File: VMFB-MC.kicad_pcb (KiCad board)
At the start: 2 copper layers, 79.1 x 83 mm, 52 parts, among them J1 DISPENSE, J12 Conn_01x10_Pin, J2 EMPTY, J3 DISPENSE, J4 DEPOSIT, J5 DISPENSE, J6 EMPTY, J7 MOTOR, J8 PIR, J9 Conn_01x04_Pin, Q1 Q_Photo_NPN, Q10 Q_Photo_NPN, Q2 Q_Photo_NPN, Q3 Q_Photo_NPN, Q4 Q_Photo_NPN, Q5 Q_Photo_NPN, Q6 Q_Photo_NPN, Q7 TIP120, Q8 TIP120, Q9 BC337, U1 LM393

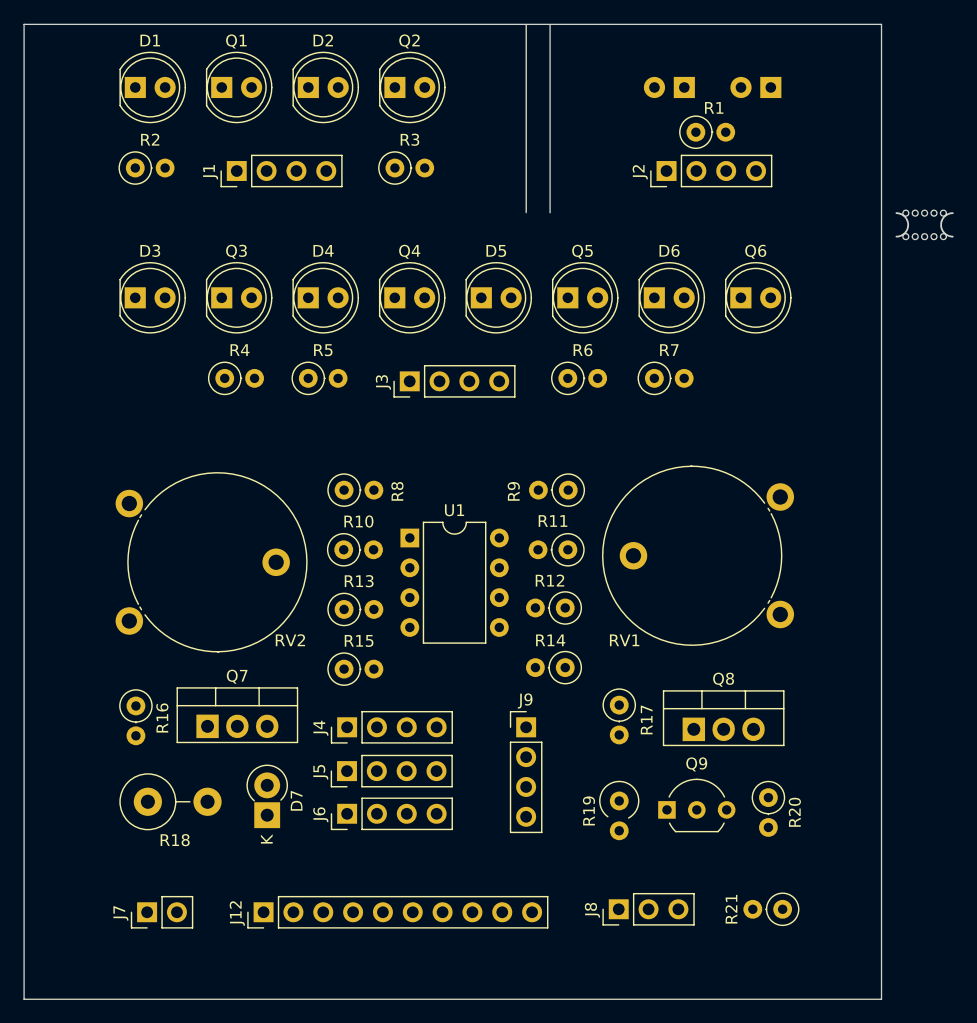
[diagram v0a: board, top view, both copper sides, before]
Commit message: New layour and routing
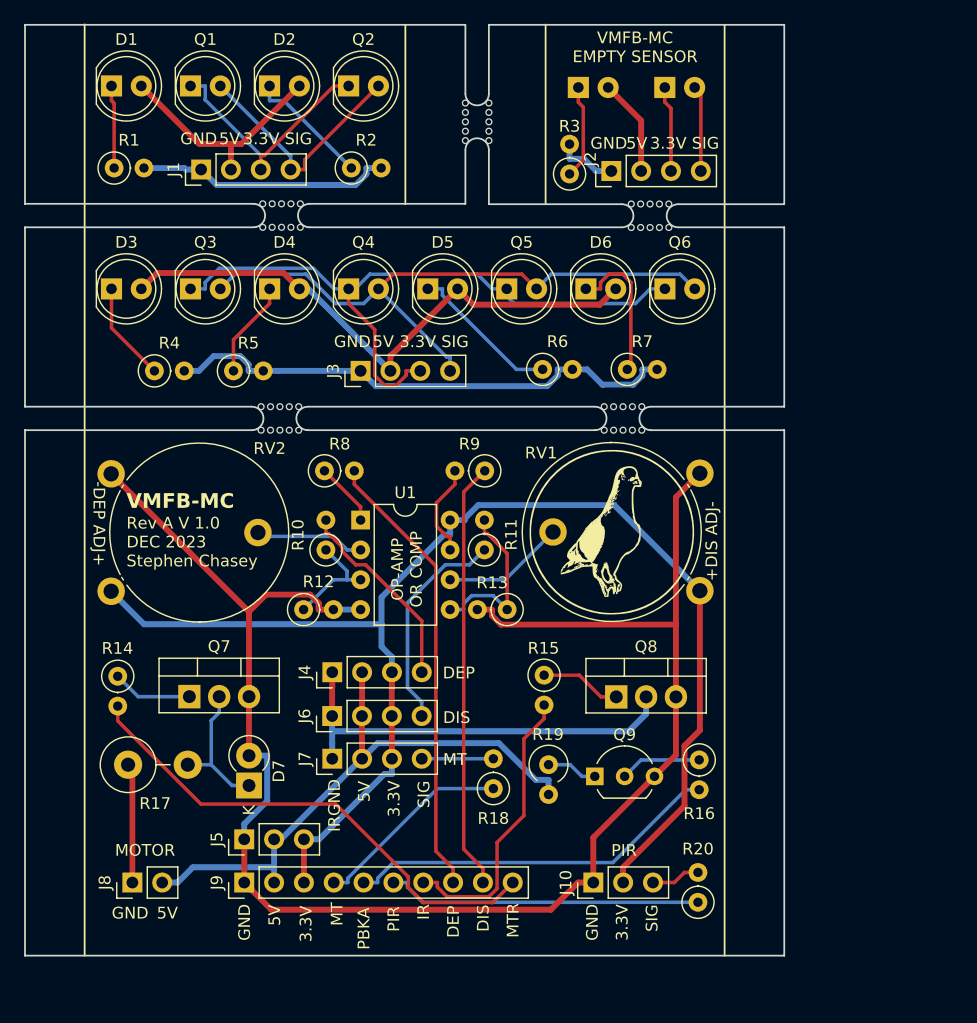
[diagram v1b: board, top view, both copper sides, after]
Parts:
- removed the J9 at (142.7, 109.8)
- removed the R10 at (127.2, 94.7)
- removed the R11 at (146.3, 94.7)
- added J5: Conn_01x03_Pin, Connector_PinHeader_2.54mm:PinHeader_1x03_P2.54mm_Vertical, F.Cu at (118.7, 119.4)
- added LOGO_BACK: LOGO, VMFB:VMFB_logo_14mm, B.Cu at (150.1, 93.2)
- added LOGO_FRONT: LOGO, VMFB:VMFB_logo_14mm, F.Cu at (150.0, 93.2)
- added R18: 10K, Resistor_THT:R_Axial_DIN0207_L6.3mm_D2.5mm_P2.54mm_Vertical, F.Cu at (140.0, 115.1)
- moved R3 11.3 mm to (146.4, 62.7), turned to 90 degrees
- moved Q10 9.03 mm to (154.5, 55.4), turned to 0 degrees
- moved D8 9.02 mm to (147.2, 55.4), turned to 0 degrees
- moved R11 8.47 mm to (139.2, 94.7), turned to 90 degrees
- moved R9 7.29 mm to (139.2, 88.0)
- moved R20 7.24 mm to (157.4, 124.7), turned to 90 degrees
- moved Q8 7.16 mm to (150.4, 107.3)
- moved RV1 7.14 mm to (157.5, 88.2)
- moved R13 6.99 mm to (141.1, 99.8)
- moved R15 6.89 mm to (144.3, 105.4)
- moved Q9 6.78 mm to (148.6, 114.0)
- moved R19 6.76 mm to (144.7, 113.0)
- moved R16 6.71 mm to (157.5, 112.6)
- moved Q6 6.51 mm to (154.6, 72.5)
- moved R5 6.40 mm to (117.8, 79.5)
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- renumbered J8 to J10, J5 to J6, J6 to J7, J7 to J8, J12 to J9, R2 to R1, R13 to R10, R12 to R11, R15 to R12, R14 to R13, R16 to R14, R17 to R15, R20 to R16, R18 to R17, R3 to R2, R21 to R20, R1 to R3
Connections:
- net Net-(D1-A) renamed DIS PWR
- net Net-(D3-A) renamed DEP PWR
- net Net-(D8-A) renamed MT PWR
- net Net-(J1-Pin_1) renamed DIS GND
- net Net-(J2-Pin_1) renamed MT GND
- net Net-(J3-Pin_1) renamed DEP GND
- J7 pad 4: EMPTY -> Net-(J7-Pin_4)
- J9 pad 2: +3.3V -> +5V
- J9 pad 3: +5V -> +3.3V
- R13 pad 1: GND -> Net-(U1B-+)
- R13 pad 2: Net-(U1B-+) -> GND
- R17 pad 1: Net-(D7-K) -> MOTOR GND
- R17 pad 2: MOTOR GND -> Net-(D7-K)
- RV1 pad 1: +3.3V -> GND
- RV1 pad 3: GND -> +3.3V
- U1 pad 2: Net-(U1A--) -> DEPOSIT ADJ
- U1 pad 6: Net-(U1B--) -> DISPENSE ADJ
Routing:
- net GND: track 0.00 -> 140.9 mm
- net +3.3V: track 0.00 -> 114.8 mm
- net Net-(J3-Pin_3): track 0.00 -> 58.1 mm
- net Net-(J3-Pin_4): track 0.00 -> 54.2 mm
- net +5V: track 0.00 -> 50.7 mm
- net DEP PWR: track 0.00 -> 49.2 mm
- net DEP GND: track 0.00 -> 44.4 mm
- net MOTOR: track 0.00 -> 42.5 mm
- net DEPOSIT: track 0.00 -> 38.5 mm
- net DISPENSE: track 0.00 -> 36.5 mm
- net IR GND: track 0.00 -> 36.2 mm
- net PBKA: track 0.00 -> 32.1 mm
- net PIR: track 0.00 -> 26.8 mm
- net SENSOR IR: track 0.00 -> 24.6 mm
- net DIS GND: track 0.00 -> 21.7 mm
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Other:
- board size 79.1 x 83 mm -> 64.6 x 79.2 mm
- board text added: "+DIS ADJ-"
- board text added: "-DEP ADJ+"
- board text added: "3.3V"
- board text added: "5V"
- board text added: "DEP"
- board text added: "DIS"
- board text added: "GND"
- board text added: "IR"
- board text added: "IRGND"
- board text added: "MOTOR"
- board text added: "MT"
- board text added: "MTR"
- board text added: "OP-AMP OR COMP"
- board text added: "PBKA"
- board text added: "PIR"
- board text added: "Rev A V 1.0 DEC 2023 Stephen Chasey"
- board text added: "SIG"
- board text added: "VMFB-MC"
- board text added: "VMFB-MC DEPOSIT SENSOR"
- board text added: "VMFB-MC DISPENSE SENSOR"
- board text added: "VMFB-MC EMPTY SENSOR"
- board text added: "VMFB-MC MAIN BOARD"

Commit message: updating netclasses, adding routing
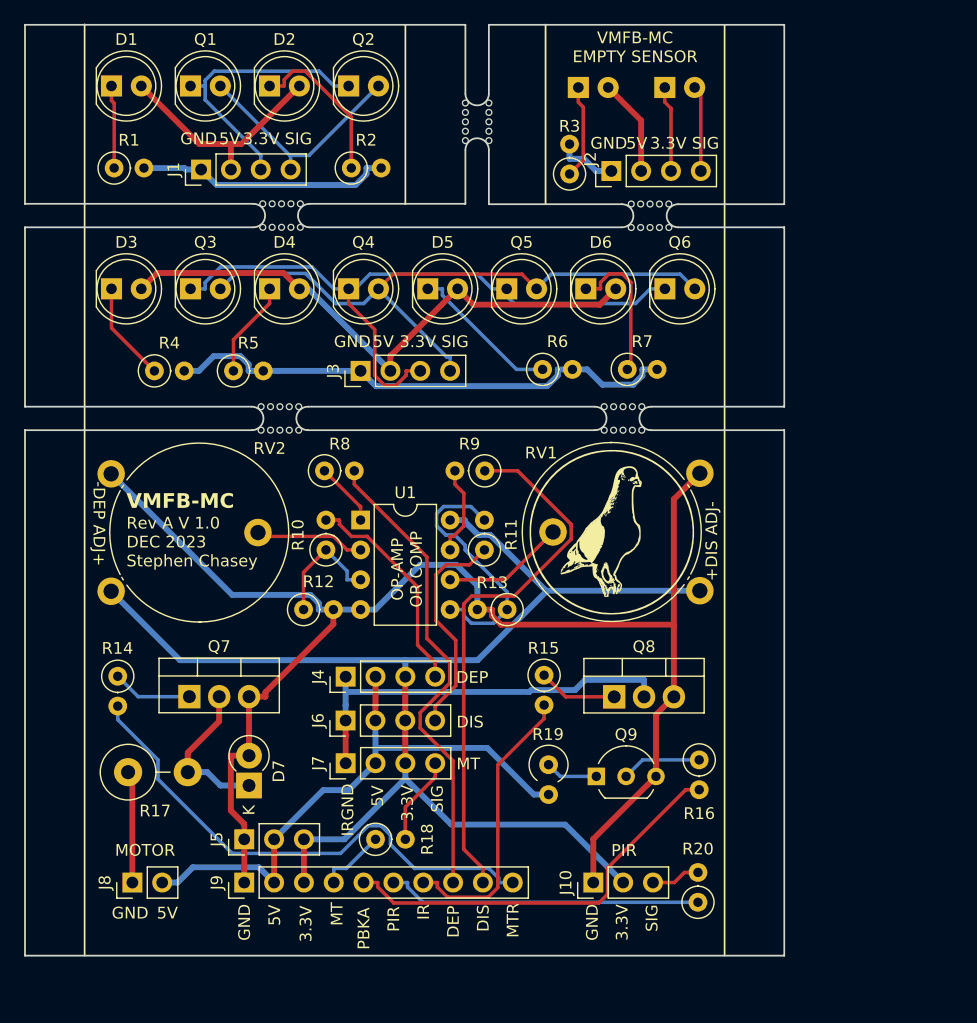
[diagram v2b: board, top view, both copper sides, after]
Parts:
- moved R18 10.9 mm to (129.9, 119.4), turned to 0 degrees
- moved J4 1.20 mm to (127.4, 105.5)
- moved J6 1.20 mm to (127.4, 109.3)
- moved J7 1.20 mm to (127.4, 112.9)
- moved R17 0.64 mm to (108.9, 113.7)
- moved Q8 0.18 mm to (150.2, 107.3)
- moved Q9 0.13 mm to (148.7, 114.0)
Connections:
- net Net-(D7-K) renamed MOTOR GND RES
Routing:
- net GND: track 140.9 -> 126.2 mm
- net EMPTY: track 17.1 -> 5.78 mm
- net DISPENSE: track 36.5 -> 46.3 mm
- net Net-(U1B-+): track 14.7 -> 22.0 mm
- net Net-(D2-K): track 10.6 -> 13.8 mm
- net PBKA: track 32.1 -> 34.8 mm
- net Net-(J1-Pin_3): track 21.4 -> 23.9 mm
- net +3.3V: track 114.8 -> 112.5 mm
- net DEPOSIT: track 38.5 -> 40.6 mm
- net DEPOSIT SIG: track 17.0 -> 18.6 mm
- net MOTOR: track 42.5 -> 44.1 mm
- net IR GND: track 36.2 -> 34.7 mm
- net Net-(J7-Pin_4): track 6.10 -> 7.53 mm
- net +5V: track 50.7 -> 49.4 mm
- net MOTOR GND RES: track 12.0 -> 13.2 mm
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
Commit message: cleaned up tracks
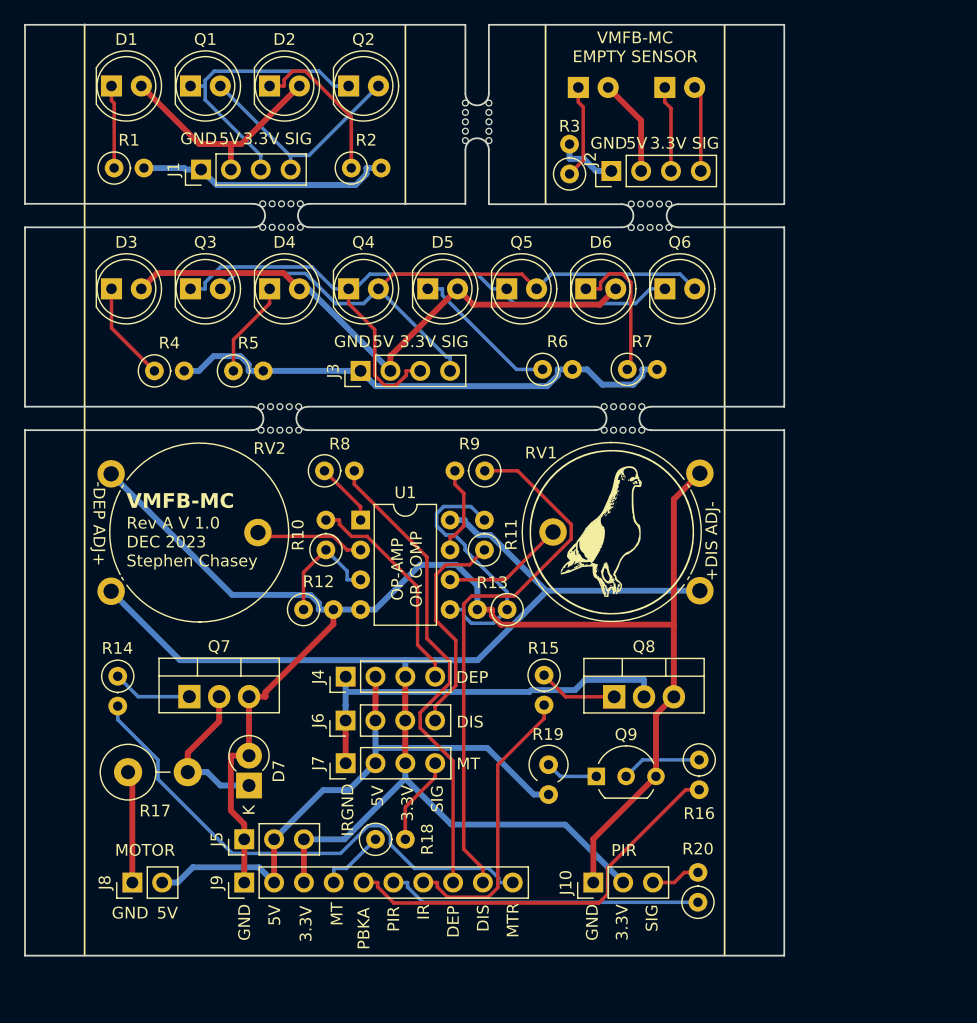
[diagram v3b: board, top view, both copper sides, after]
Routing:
- net Net-(J3-Pin_3): track 58.2 -> 57.0 mm
- net MOTOR GND: track 9.55 -> 9.03 mm
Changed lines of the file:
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@@
     (effects (font (size 1 1) (thickness 0.15)) (justify left bottom))
   )
-  (segment (start 108.856 113.665) (end 109.22 114.029) (width 0.5) (layer "F.Cu") (net 1))
   (segment (start 109.22 114.029) (end 109.22 123.063) (width 0.5) (layer "F.Cu") (net 1))
   (segment (start 119.882 107.2355) (end 120.5536 107.2355) (width 0.5) (layer "F.Cu") (net 2))
@@
   (segment (start 149.0781 72.517) (end 149.0781 71.9701) (width 0.3) (layer "F.Cu") (net 5))
   (segment (start 149.8048 71.2434) (end 150.9316 71.2434) (width 0.3) (layer "F.Cu") (net 5))
-  (segment (start 151.6608 79.0692) (end 151.355 79.375) (width 0.3) (layer "F.Cu") (net 5))
   (segment (start 147.828 72.517) (end 149.0781 72.517) (width 0.3) (layer "F.Cu") (net 5))
   (segment (start 149.0781 71.9701) (end 149.8048 71.2434) (width 0.3) (layer "F.Cu") (net 5))
@@
   (segment (start 128.651 94.742) (end 127.5009 94.742) (width 0.3) (layer "F.Cu") (net 19))
   (segment (start 126.3508 93.5919) (end 120.2394 93.5919) (width 0.3) (layer "F.Cu") (net 19))
-  (segment (start 120.2394 93.5919) (end 119.913 93.2655) (width 0.3) (layer "F.Cu") (net 19))
   (segment (start 139.065 123.063) (end 139.065 121.8629) (width 0.3) (layer "F.Cu") (net 20))
   (segment (start 138.1058 98.6718) (end 141.7381 98.6718) (width 0.3) (layer "F.Cu") (net 20))
@@
   (segment (start 107.442 56.4951) (end 107.667 56.7201) (width 0.3) (layer "F.Cu") (net 26))
   (segment (start 107.442 55.245) (end 107.442 56.4951) (width 0.3) (layer "F.Cu") (net 26))
-  (segment (start 117.612 61.0569) (end 117.612 60.1872) (width 0.5) (layer "F.Cu") (net 27))
+  (segment (start 117.612 62.357) (end 117.612 60.1872) (width 0.5) (layer "F.Cu") (net 27))
   (segment (start 118.4968 60.1872) (end 117.612 60.1872) (width 0.5) (layer "F.Cu") (net 27))
   (segment (start 123.439 55.245) (end 118.4968 60.1872) (width 0.5) (layer "F.Cu") (net 27))
-  (segment (start 117.612 62.357) (end 117.612 61.0569) (width 0.5) (layer "F.Cu") (net 27))
   (segment (start 114.9242 60.1872) (end 109.982 55.245) (width 0.5) (layer "F.Cu") (net 27))
   (segment (start 117.612 60.1872) (end 114.9242 60.1872) (width 0.5) (layer "F.Cu") (net 27))
@@
   (segment (start 152.6449 79.893) (end 152.6449 79.375) (width 0.5) (layer "B.Cu") (net 38))
   (segment (start 145.4349 79.893) (end 145.4349 79.375) (width 0.5) (layer "B.Cu") (net 38))
-  (segment (start 128.651 79.502) (end 121.6171 79.502) (width 0.5) (layer "B.Cu") (net 38))
+  (segment (start 120.367 79.502) (end 128.651 79.502) (width 0.5) (layer "B.Cu") (net 38))
   (segment (start 153.895 79.375) (end 152.6449 79.375) (width 0.5) (layer "B.Cu") (net 38))
-  (segment (start 120.367 79.502) (end 121.6171 79.502) (width 0.5) (layer "B.Cu") (net 38))
   (segment (start 130.7102 80.741) (end 129.8512 79.882) (width 0.3) (layer "F.Cu") (net 39))
   (segment (start 129.8512 79.882) (end 129.8512 75.9883) (width 0.3) (layer "F.Cu") (net 39))
@@
   (segment (start 133.731 79.502) (end 132.5309 79.502) (width 0.3) (layer "F.Cu") (net 39))
   (segment (start 132.5309 79.877) (end 131.6669 80.741) (width 0.3) (layer "F.Cu") (net 39))
-  (segment (start 127.63 72.517) (end 128.193 72.517) (width 0.3) (layer "B.Cu") (net 39))
   (segment (start 140.467 72.517) (end 141.7171 73.7671) (width 0.3) (layer "B.Cu") (net 39))
   (segment (start 116.731 70.6572) (end 115.4181 71.9701) (width 0.3) (layer "B.Cu") (net 39))
@@
   (segment (start 114.168 72.517) (end 115.4181 72.517) (width 0.3) (layer "B.Cu") (net 39))
   (segment (start 154.559 72.517) (end 153.3089 72.517) (width 0.3) (layer "B.Cu") (net 39))
-  (segment (start 141.092 72.517) (end 140.467 72.517) (width 0.3) (layer "B.Cu") (net 39))
   (segment (start 127.63 72.517) (end 126.3799 72.517) (width 0.3) (layer "B.Cu") (net 39))
   (segment (start 142.3818 71.2668) (end 143.632 72.517) (width 0.3) (layer "F.Cu") (net 40))

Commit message: layout update
updates layout to compress it a bit.
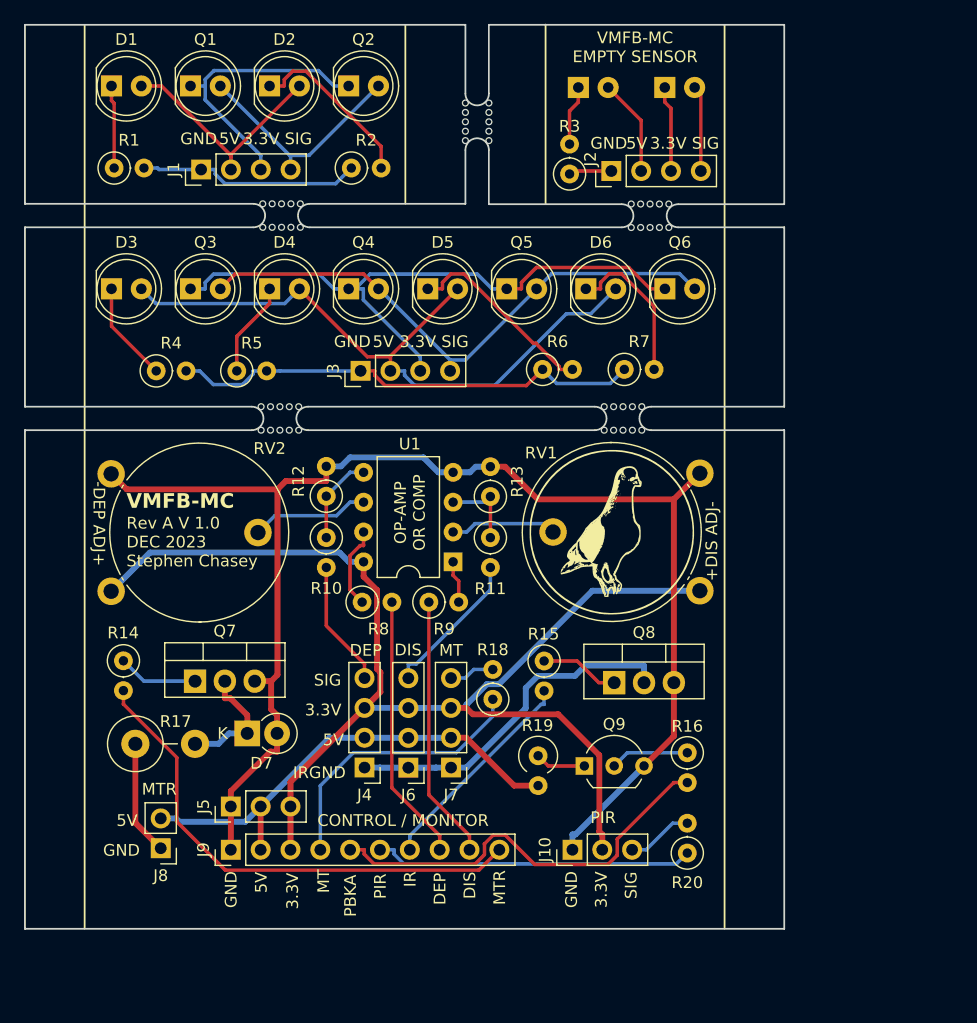
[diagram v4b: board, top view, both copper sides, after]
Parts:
- D1, D2, D3, D4, D5, D6, D8: value CQY99 -> IR LED
- R1, R2, R4, R5, R6, R7: value 100R -> 150R
- R3: value 100R -> 1K
- moved R18 15.5 mm to (139.9, 107.5), turned to 90 degrees
- moved R9 12.1 mm to (134.5, 99.2), turned to 0 degrees
- moved R8 11.6 mm to (128.8, 99.2)
- moved R12 9.84 mm to (125.7, 90.2), turned to 90 degrees
- moved R13 9.73 mm to (139.7, 90.2), turned to 90 degrees
- moved J7 8.98 mm to (136.4, 113.3), turned to 180 degrees
- moved U1 8.64 mm to (136.5, 95.8), turned to 180 degrees
- moved J4 7.90 mm to (129.0, 113.3), turned to 180 degrees
- moved J6 6.69 mm to (132.7, 113.3), turned to 180 degrees
- moved D7 4.44 mm to (119.0, 110.4), turned to 0 degrees
- moved R20 4.29 mm to (156.5, 120.6)
- moved J8 3.79 mm to (111.6, 120.1), turned to 180 degrees
- moved J10 3.31 mm to (146.7, 120.3)
- moved J5 3.02 mm to (117.6, 116.6)
- moved J9 3.02 mm to (117.6, 120.3)
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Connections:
- net DEP PWR renamed Net-(D3-A)
- net DIS PWR renamed Net-(D1-A)
- net MT PWR renamed Net-(D8-A)
- J1 pad 1: DIS GND -> Net-(J1-Pin_1)
- J2 pad 1: MT GND -> Net-(J2-Pin_1)
- J3 pad 1: DEP GND -> Net-(J3-Pin_1)
- R1 pad 2: DIS GND -> Net-(J1-Pin_1)
- R10 pad 1: Net-(U1A-+) -> Net-(U1B-+)
- R11 pad 1: DISPENSE SIG -> Net-(U1A-+)
- R11 pad 2: Net-(U1B-+) -> DISPENSE SIG
- R12 pad 1: Net-(U1A-+) -> Net-(U1B-+)
- R13 pad 1: Net-(U1B-+) -> Net-(U1A-+)
- R2 pad 1: Net-(D2-K) -> Net-(J1-Pin_1)
- R2 pad 2: DIS GND -> Net-(D2-K)
- R3 pad 1: Net-(D8-K) -> Net-(J2-Pin_1)
- R3 pad 2: MT GND -> Net-(D8-K)
- R4 pad 2: DEP GND -> Net-(J3-Pin_1)
- R5 pad 2: DEP GND -> Net-(J3-Pin_1)
- R6 pad 1: Net-(D5-K) -> Net-(J3-Pin_1)
- R6 pad 2: DEP GND -> Net-(D5-K)
- R7 pad 1: Net-(D6-K) -> Net-(J3-Pin_1)
- R7 pad 2: DEP GND -> Net-(D6-K)
- U1 pad 1: Net-(R8-Pad1) -> Net-(R9-Pad2)
- U1 pad 2: DEPOSIT ADJ -> DISPENSE ADJ
- U1 pad 6: DISPENSE ADJ -> DEPOSIT ADJ
- U1 pad 7: Net-(R9-Pad2) -> Net-(R8-Pad1)
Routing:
- net DEP GND: track 44.4 -> 0.00 mm
- net Net-(J3-Pin_1): track 0.00 -> 40.7 mm
- net DISPENSE: track 46.3 -> 22.5 mm
- net DIS GND: track 21.7 -> 0.00 mm
- net Net-(J1-Pin_1): track 0.00 -> 19.0 mm
- net EMPTY: track 5.78 -> 24.0 mm
- net DEPOSIT: track 40.6 -> 22.8 mm
- net Net-(U1B-+): track 22.0 -> 7.55 mm
- net +5V: track 49.4 -> 40.6 mm
- net Net-(D3-A): track 49.2 -> 57.3 mm
- net DEPOSIT SIG: track 18.6 -> 10.8 mm
- net SENSOR IR: track 24.6 -> 18.4 mm
- net DISPENSE SIG: track 18.8 -> 12.7 mm
- net Net-(J3-Pin_4): track 54.3 -> 48.5 mm
- net +3.3V: track 112.5 -> 106.7 mm
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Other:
- board size 64.6 x 79.2 mm -> 64.6 x 77 mm
- board text added: "CONTROL / MONITOR"
- board text removed: "MOTOR"
